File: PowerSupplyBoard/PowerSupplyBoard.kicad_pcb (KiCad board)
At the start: 4 copper layers, 50 x 75 mm, 80 parts, among them J101 BATTERY, J102 DATA2, J103 USB_C, J104 PWR, J105 DATA1, J106 USB_B_Micro, Q101 BSH205G2A, Q102 TD6790, Q103 TD6790, Q104 TD6790, SW101 SW_SPDT, U101 TPS63021, U102 MCP73834T, U103 TC7662Bx0A, U104 TC7662Bx0A, U105 CS5173

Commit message: Power board rev 3
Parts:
- removed C117, C118: 1u, Capacitor_SMD:C_0805_2012Metric
- removed C119, C120: 100n, Capacitor_SMD:C_0805_2012Metric
- removed D108: PMEG3030, Diode_SMD:D_SOD-123
- removed D110: SP0503BAHT, Package_TO_SOT_SMD:SOT-143
- removed J102: DATA2, Connector_PinHeader_2.54mm:PinHeader_1x02_P2.54mm_Vertical
- removed J106: USB_B_Micro, Connector_USB:USB_Micro-B_Amphenol_10118193-0001LF_Horizontal
- removed JP101: DIG_CM, Jumper:SolderJumper-2_Open_TrianglePad_0805
- removed JP102, JP103: INV_HIFREQ, Jumper:SolderJumper-2_Open_TrianglePad_0805
- removed JP104: POS_CM, Jumper:SolderJumper-2_Open_TrianglePad_0805
- removed JP105: NEG_CM, Jumper:SolderJumper-2_Open_TrianglePad_0805
- removed Q102, Q103, Q104: TD6790, PCM_4ms_Package_SOIC:SM-8
- removed TP104: -12A, TestPoint:TestPoint_Pad_D1.0mm_Value
- removed TP106: -12V, TestPoint:TestPoint_Pad_D1.0mm_Value
- removed TP107: +12V, TestPoint:TestPoint_Pad_D1.0mm_Value
- removed U104: TC7662Bx0A, Package_DIP:DIP-8_W7.62mm
- added L103: 22uH, Inductor_SMD:L_Changjiang_FNR4010S, F.Cu at (27.9, 56.2)
- added R116: 330k, Resistor_SMD:R_0805_2012Metric, F.Cu at (18.9, 51.5)
- added R117: 100k, Resistor_SMD:R_0805_2012Metric, F.Cu at (23.0, 51.5)
- added RV101: 10k, Potentiometer_THT:Potentiometer_Bourns_3296W_Vertical, F.Cu at (28.9, 49.3)
- added RV102: 10k, Potentiometer_THT:Potentiometer_Bourns_3296W_Vertical, F.Cu at (26.5, 64.3)
- C103: value 22u -> 100n
- C107: value 100n -> 22u
- C111: value 10u -> 4u7
- C112: value 10u -> 4n7
- C113: value 10u -> 2u2
- R103: value 10k -> 1k
- R111: value 4k7 -> 470k
- R112: value 12k -> 33k
- R113: value 12k -> 4k7
- TP101: value 3V3 -> -12
- TP102: value 3V3P -> 3V3
- TP105: value +12A -> +12
- U103: value TC7662Bx0A -> MAX17578ATC; footprint Package_DIP:DIP-8_W7.62mm -> Package_DFN_QFN:TDFN-12-1EP_3x3mm_P0.4mm_EP1.7x2.45mm
- moved TP101 49.6 mm to (13.4, 65.0), turned to 180 degrees
- moved C107 32.4 mm to (12.4, 62.2), turned to 0 degrees
- moved R111 28.1 mm to (23.2, 59.3), turned to 180 degrees
- moved C103 26.8 mm to (32.6, 56.5), turned to 90 degrees
- moved TP105 26.2 mm to (12.9, 40.6), turned to 180 degrees
- moved D107 25.0 mm to (19.7, 23.2)
- moved R102 23.4 mm to (11.6, 13.5), turned to -90 degrees
- moved R109 22.2 mm to (16.8, 46.6), turned to 180 degrees
- moved C112 21.5 mm to (15.4, 59.0), turned to -90 degrees
- moved R113 20.8 mm to (15.4, 55.2), turned to 90 degrees
- moved R105 19.9 mm to (13.1, 9.84), turned to 90 degrees
- moved C116 19.8 mm to (16.1, 43.6), turned to -90 degrees
- moved D106 19.6 mm to (16.1, 39.2), turned to 90 degrees
- moved C113 17.4 mm to (18.8, 59.0), turned to -90 degrees
- moved Q101 14.6 mm to (20.0, 13.0), turned to 0 degrees
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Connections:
- C103 pad 1: Net-(Q102A-B1) -> Net-(U103-BST)
- C103 pad 2: GND -> Net-(U103-LX)
- C107 pad 1: +3.3V -> GND
- C107 pad 2: GND -> -12V
- C108 pad 1: +3.3VP -> +3.3V
- C111 pad 1: Net-(U103-CAP+) -> +12V
- C111 pad 2: Net-(U103-CAP-) -> GND
- C112 pad 1: Net-(U104-CAP+) -> Net-(U103-SS)
- C112 pad 2: Net-(U104-CAP-) -> -12V
- C113 pad 1: -12VA -> Net-(U103-VCC)
- C113 pad 2: GND -> -12V
- C116 pad 1: +12VA -> +12V
- D106 pad 1: +12VA -> +12V
- R103 pad 1: +3.3VP -> Net-(R103-Pad1)
- R103 pad 2: Net-(Q102A-B1) -> GND
- R105 pad 1: +3.3VP -> +3.3V
- R110 pad 1: +12VA -> +12V
- R111 pad 1: Net-(U105-FB) -> GND
- R111 pad 2: GND -> Net-(U103-FB)
- R112 pad 1: -12VA -> Net-(R112-Pad1)
- R112 pad 2: Net-(Q103B-B2) -> -12V
- R113 pad 1: +12VA -> /NRST
- R113 pad 2: Net-(Q104A-B1) -> +3.3V
- TP101 pad 1: +3.3V -> -12V
- TP102 pad 1: +3.3VP -> +3.3V
- TP105 pad 1: +12VA -> +12V
- U101 pad 3: +3.3VP -> +3.3V
- U101 pad 4: +3.3VP -> +3.3V
- U101 pad 5: +3.3VP -> +3.3V
- U103 pad 1: Net-(JP102-A) -> +12V
- U103 pad 2: Net-(U103-CAP+) -> Net-(U103-EN/UVLO)
- U103 pad 3: GND -> /NRST
- U103 pad 4: Net-(U103-CAP-) -> Net-(U103-SS)
- U103 pad 5: -12VA -> Net-(U103-VCC)
- U103 pad 7: unconnected-(U103-OSC-Pad7) -> Net-(U103-FB)
- U103 pad 8: +12V -> -12V
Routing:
- net -12VA: track 70.5 -> 0.00 mm
- net USBM_D-: track 59.5 -> 0.00 mm, vias 1 -> 0
- net USBM_D+: track 58.8 -> 0.00 mm, vias 1 -> 0
- net +3.3V: track 89.8 -> 128.1 mm, vias 0 -> 2
- net +12VA: track 37.4 -> 0.00 mm
- net VDD: track 62.4 -> 34.2 mm, vias 0 -> 2
- net GND: track 68.5 -> 40.7 mm, vias 155 -> 189
- net Net-(D107-A): track 23.5 -> 49.9 mm
- net +3.3VP: track 25.6 -> 0.00 mm
- net -12V: track 71.3 -> 47.9 mm
- net Net-(D105-A): track 25.9 -> 5.85 mm, vias 1 -> 0
- net USBC_D+: track 89.5 -> 108.0 mm, vias 2 -> 3
- net USBC_D-: track 92.9 -> 110.2 mm, vias 2 -> 3
- net V_PWR: track 30.2 -> 46.7 mm
- net +12V: track 57.9 -> 41.4 mm
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- added copper zone on B.Cu, net GND
- added copper zone on F.Cu, net GND
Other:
- board outline removed
- board text removed: "Rev. 2 July 2024 Hayden Setlik"
- board text removed: "USB Synth Power Supply"

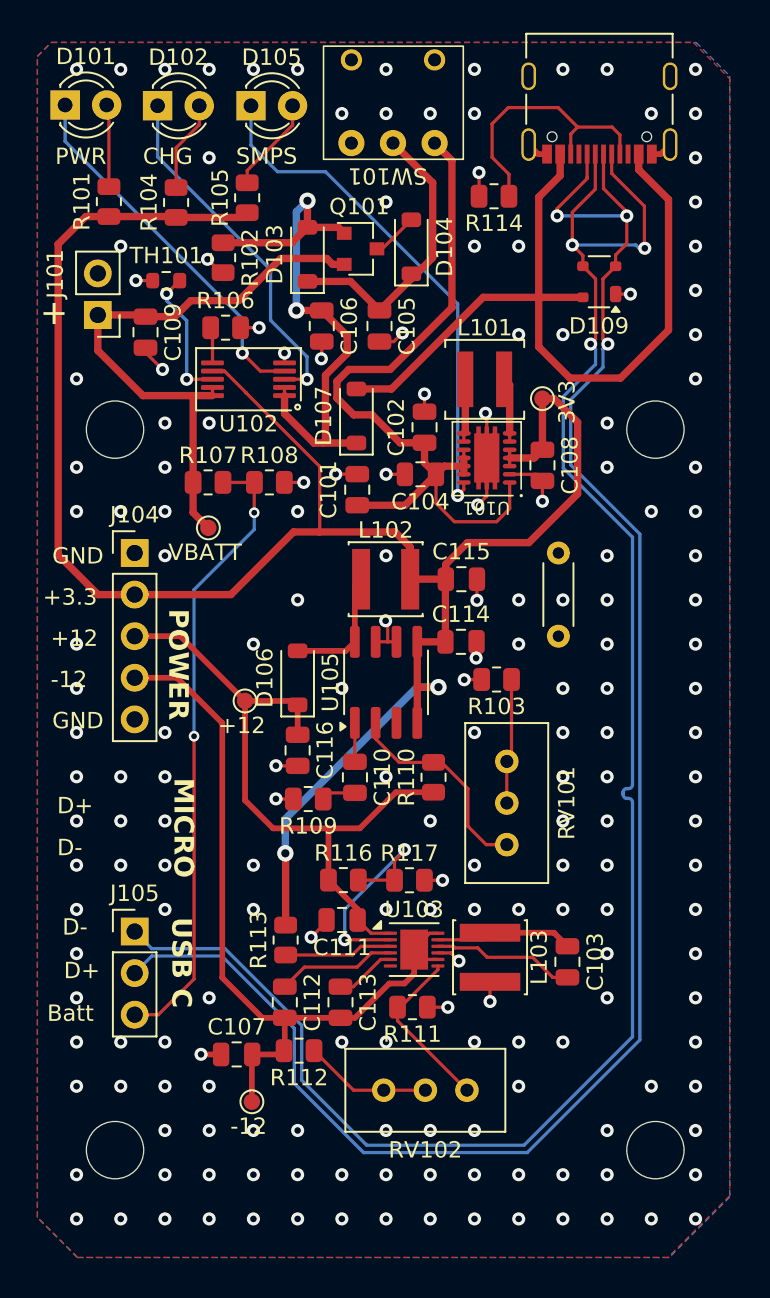
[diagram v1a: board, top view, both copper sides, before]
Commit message: psu rev 3 sent to fab
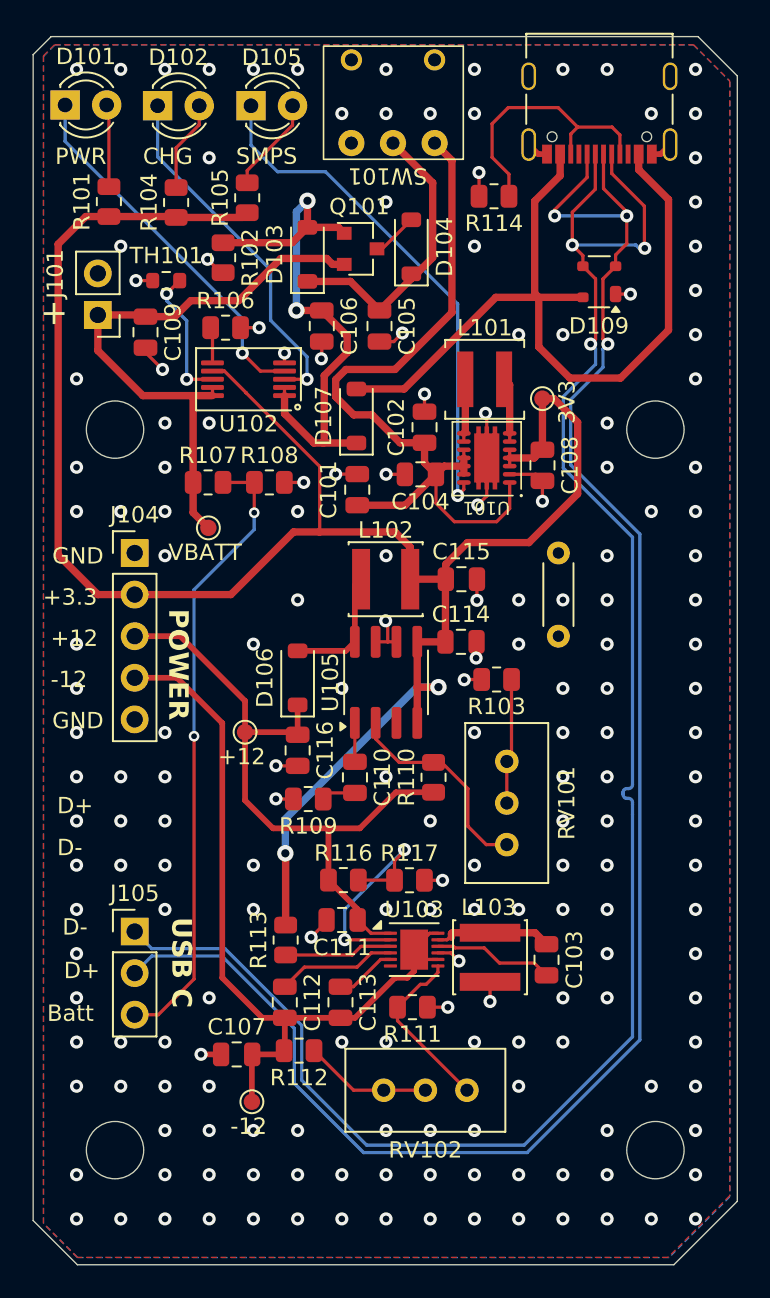
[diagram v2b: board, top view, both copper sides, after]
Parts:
- moved TP105 1.91 mm to (12.9, 42.5)
- moved C103 1.28 mm to (31.4, 56.4)
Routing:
- net Net-(U103-BST): track 8.69 -> 7.37 mm
- net Net-(U103-LX): track 8.43 -> 7.15 mm
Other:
- board outline added: 43 x 75 mm
- board text added: "Rev. 3 July 2024 Hayden Setlik"
- board text added: "USB Synth Power Supply"
- board text removed: "MICRO"

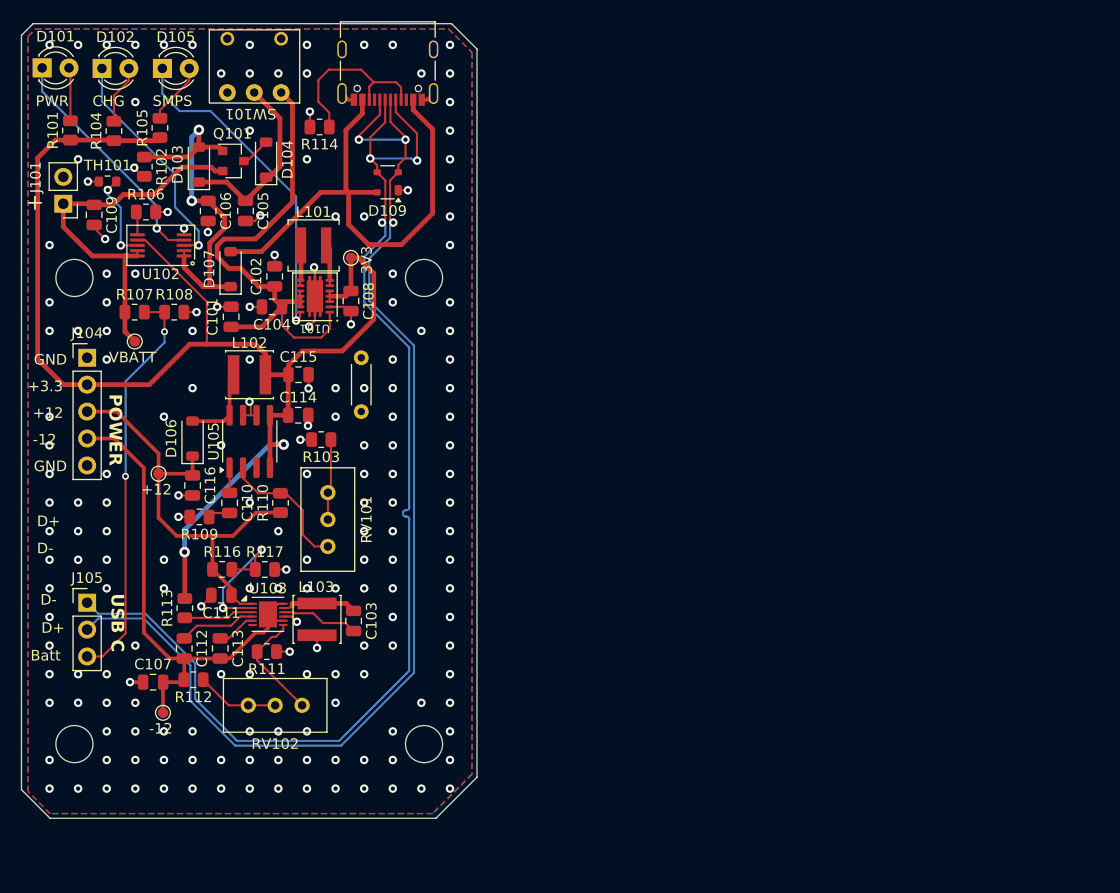
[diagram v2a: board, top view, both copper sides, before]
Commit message: PSU rev4 schematic
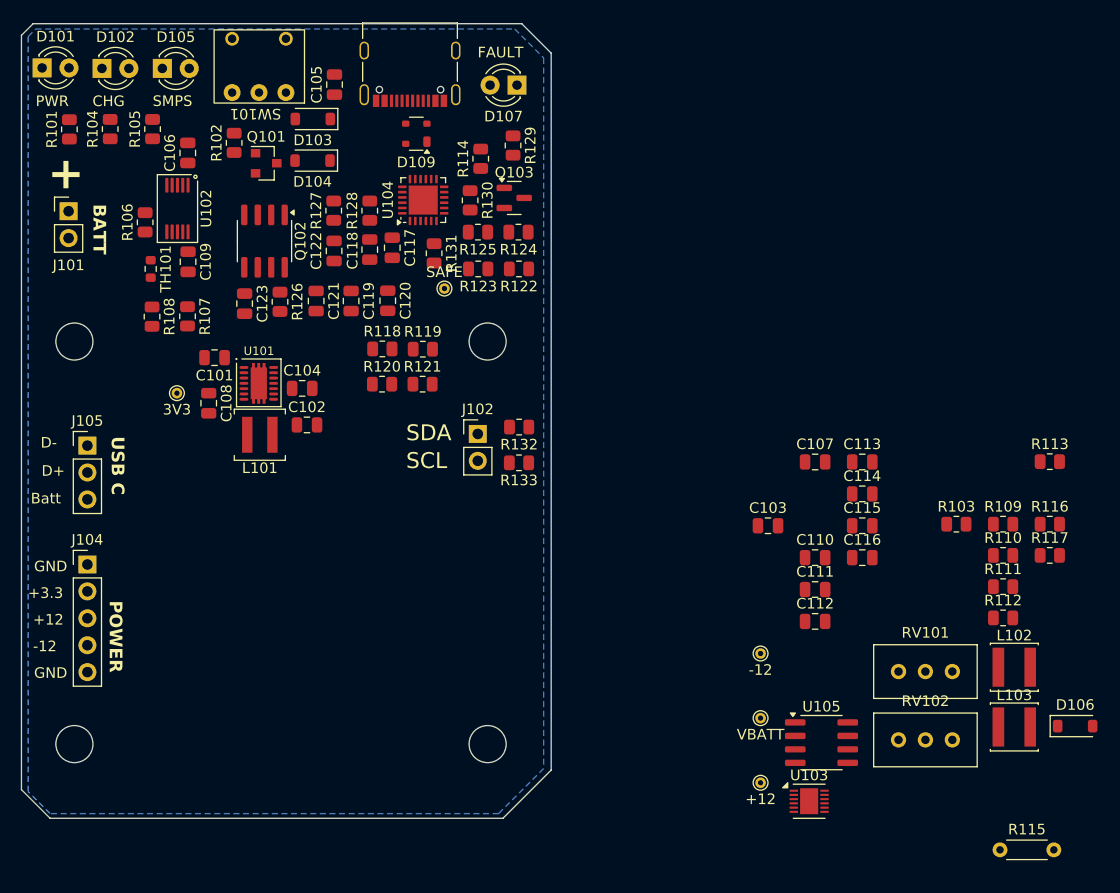
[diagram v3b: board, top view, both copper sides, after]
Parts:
- added C117: 4u7, Capacitor_SMD:C_0805_2012Metric, F.Cu at (35.0, 21.1)
- added C118: 100n, Capacitor_SMD:C_0805_2012Metric, F.Cu at (32.9, 21.3)
- added C119: 100n, Capacitor_SMD:C_0805_2012Metric, F.Cu at (31.1, 26.2)
- added C120: 4u7, Capacitor_SMD:C_0805_2012Metric, F.Cu at (34.6, 26.1)
- added C121: 4u7, Capacitor_SMD:C_0805_2012Metric, F.Cu at (27.8, 26.2)
- added C122: 100n, Capacitor_SMD:C_0805_2012Metric, F.Cu at (29.5, 21.4)
- added C123: 1u, Capacitor_SMD:C_0805_2012Metric, F.Cu at (21.1, 26.4)
- added J102: I2C, Connector_PinHeader_2.54mm:PinHeader_1x02_P2.54mm_Vertical, F.Cu at (43.1, 38.7)
- added Q102: DMP6050SSD, Package_SO:SOIC-8_3.9x4.9mm_P1.27mm, F.Cu at (22.9, 20.5)
- added Q103: 2N7002H, Package_TO_SOT_SMD:SOT-23, F.Cu at (46.5, 16.4)
- added R118: DNP, Resistor_SMD:R_0805_2012Metric, F.Cu at (34.1, 30.7)
- added R119: 100, Resistor_SMD:R_0805_2012Metric, F.Cu at (37.9, 30.7)
- added R120: DNP, Resistor_SMD:R_0805_2012Metric, F.Cu at (34.0, 34.0)
- added R121: 100, Resistor_SMD:R_0805_2012Metric, F.Cu at (37.9, 34.0)
- added R122: 10k, Resistor_SMD:R_0805_2012Metric, F.Cu at (47.0, 23.1)
- added R123: 5k1, Resistor_SMD:R_0805_2012Metric, F.Cu at (43.1, 23.1)
- added R124: DNP, Resistor_SMD:R_0805_2012Metric, F.Cu at (46.9, 19.7)
- added R125: 100, Resistor_SMD:R_0805_2012Metric, F.Cu at (43.1, 19.7)
- added R126: 22k, Resistor_SMD:R_0805_2012Metric, F.Cu at (24.4, 26.2)
- added R127: 2k2, Resistor_SMD:R_0805_2012Metric, F.Cu at (29.5, 17.6)
- added R128: 2k2, Resistor_SMD:R_0805_2012Metric, F.Cu at (32.9, 17.6)
- added R129: 10k, Resistor_SMD:R_0805_2012Metric, F.Cu at (46.4, 11.5)
- added R130: 10k, Resistor_SMD:R_0805_2012Metric, F.Cu at (42.4, 16.7)
- added R131: 2k2, Resistor_SMD:R_0805_2012Metric, F.Cu at (39.0, 21.7)
- added R132: 2k2, Resistor_SMD:R_0805_2012Metric, F.Cu at (47.0, 38.1)
- added R133: 2k2, Resistor_SMD:R_0805_2012Metric, F.Cu at (47.0, 41.5)
- added TP104: SAFE, TestPoint:TestPoint_THTPad_D1.0mm_Drill0.5mm_VAL, F.Cu at (39.9, 25.0)
- added U104: CYPD3177-24LQ, Package_DFN_QFN:QFN-24-1EP_4x4mm_P0.5mm_EP2.75x2.75mm, F.Cu at (37.9, 16.7)
- D107: value PMEG3030 -> USB; footprint Diode_SMD:D_SOD-123 -> LED_THT:LED_D3.0mm
- TP101, TP102, TP103, TP105: footprint TestPoint:TestPoint_Pad_D1.0mm_Value -> TestPoint:TestPoint_THTPad_D1.0mm_Drill0.5mm_VAL
- moved D106 87.6 mm to (99.5, 66.3), turned to 0 degrees
- moved R113 82.8 mm to (97.1, 41.3), turned to 0 degrees
- moved R116 78.2 mm to (97.1, 47.2)
- moved L102 77.3 mm to (93.7, 60.7)
- moved R112 76.6 mm to (92.7, 56.1), turned to 0 degrees
- moved R109 75.9 mm to (92.7, 47.2), turned to 0 degrees
- moved R117 74.1 mm to (97.1, 50.2)
- moved R115 73.1 mm to (92.4, 78.0), turned to 0 degrees
- moved R111 69.8 mm to (92.7, 53.1), turned to 0 degrees
- moved TP103 68.9 mm to (69.8, 65.5), turned to 0 degrees
- moved R110 68.4 mm to (92.7, 50.2), turned to 0 degrees
- moved L103 66.6 mm to (93.7, 66.4), turned to 0 degrees
- moved C107 65.9 mm to (74.9, 41.4)
- moved TP105 63.9 mm to (69.8, 71.7), turned to 0 degrees
- moved C116 63.6 mm to (79.4, 50.4), turned to 0 degrees
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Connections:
- C114 pad 1: +3.3V -> V_PWR
- C115 pad 1: +3.3V -> V_PWR
- D107 pad 1: VDD -> Net-(D107-K)
- D107 pad 2: Net-(D107-A) -> +3.3V
- D109 pad 4: Net-(D107-A) -> /VBUS
- J103 pad A4: Net-(D107-A) -> /VBUS
- J103 pad A5: Net-(J103-CC1) -> /CC1
- J103 pad A9: Net-(D107-A) -> /VBUS
- J103 pad B4: Net-(D107-A) -> /VBUS
- J103 pad B5: Net-(J103-CC1) -> /CC2
- J103 pad B9: Net-(D107-A) -> /VBUS
- L102 pad 2: +3.3V -> V_PWR
- R114 pad 1: Net-(J103-CC1) -> Net-(U104-FLIP)
- R114 pad 2: GND -> +3.3V
- SW101 pad 1: V_PWR -> VCC
- SW101 pad 2: VCC -> V_PWR
- U105 pad 4: +3.3V -> V_PWR
- U105 pad 5: +3.3V -> V_PWR
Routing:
- net +3.3V: track 128.1 -> 0.00 mm, vias 2 -> 0
- net USBC_D-: track 110.2 -> 0.00 mm, vias 3 -> 0
- net USBC_D+: track 108.0 -> 0.00 mm, vias 3 -> 0
- net Net-(D107-A): track 50.1 -> 0.00 mm
- net -12V: track 47.8 -> 0.00 mm
- net V_PWR: track 47.0 -> 0.00 mm
- net +12V: track 41.7 -> 0.00 mm
- net GND: track 40.7 -> 0.00 mm, vias 189 -> 0
- net BATT_REF: track 38.3 -> 0.00 mm, vias 2 -> 0
- net VBATT: track 36.0 -> 0.00 mm
- net VDD: track 34.2 -> 0.00 mm, vias 2 -> 0
- net Net-(D105-K): track 31.7 -> 0.00 mm, vias 1 -> 0
- net Net-(D101-K): track 22.7 -> 0.00 mm, vias 1 -> 0
- net Net-(D102-K): track 21.9 -> 0.00 mm, vias 1 -> 0
- net VCC: track 17.9 -> 0.00 mm
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- removed copper zone on F.Cu, net GND
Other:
- board size 43 x 75 mm -> 50 x 75 mm
- board text added: "BATT"
- board text added: "FAULT"
- board text added: "SCL"
- board text added: "SDA"

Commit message: routing v1
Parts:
- moved R113 85.2 mm to (14.9, 63.8), turned to 180 degrees
- moved R116 83.2 mm to (14.9, 60.6)
- moved R117 82.4 mm to (14.9, 57.2), turned to 180 degrees
- moved D106 81.7 mm to (19.5, 50.0), turned to 90 degrees
- moved L102 79.0 mm to (16.3, 44.8), turned to 90 degrees
- moved TP103 79.0 mm to (8.75, 15.4), turned to 180 degrees
- moved L103 66.4 mm to (27.7, 59.3)
- moved C113 64.9 mm to (19.1, 65.5)
- moved R109 64.4 mm to (28.5, 41.8), turned to 180 degrees
- moved R110 64.3 mm to (28.4, 50.2)
- moved C115 63.0 mm to (16.8, 40.0), turned to 90 degrees
- moved R112 60.2 mm to (33.4, 66.7), turned to 180 degrees
- moved C114 59.3 mm to (20.2, 40.0), turned to 90 degrees
- moved R111 59.3 mm to (33.4, 54.3)
- moved C111 57.9 mm to (17.0, 54.3), turned to 90 degrees
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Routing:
- net +3.3V: track 0.00 -> 200.7 mm, vias 0 -> 4
- net V_PWR: track 0.00 -> 92.9 mm, vias 0 -> 2
- net VDD: track 0.00 -> 84.9 mm, vias 0 -> 2
- net USBC_D+: track 0.00 -> 71.3 mm, vias 0 -> 3
- net USBC_D-: track 0.00 -> 69.3 mm, vias 0 -> 3
- net GND: track 0.00 -> 63.3 mm, vias 0 -> 38
- net VBATT: track 0.00 -> 51.2 mm, vias 0 -> 1
- net -12V: track 0.00 -> 46.8 mm
- net SCL: track 0.00 -> 46.3 mm, vias 0 -> 1
- net SDA: track 0.00 -> 41.7 mm, vias 0 -> 1
- net Net-(D105-K): track 0.00 -> 39.2 mm, vias 0 -> 3
- net +12V: track 0.00 -> 34.5 mm
- net /CC2: track 0.00 -> 27.6 mm
- net Net-(U103-FB): track 0.00 -> 20.9 mm
- net Net-(C121-Pad2): track 0.00 -> 20.1 mm
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- added copper zone on F.Cu, net /VBUS
